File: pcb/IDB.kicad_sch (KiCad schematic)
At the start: 38 parts, among them J1 Conn_01x10_Socket, J10 Conn_01x03_Socket, J11 Conn_01x03_Socket, J12 Conn_01x03_Socket, J13 Conn_01x03_Socket, J14 Conn_01x03_Socket, J15 Conn_01x03_Socket, J16 Conn_01x03_Socket, J17 Conn_01x03_Socket, J18 Conn_01x03_Socket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

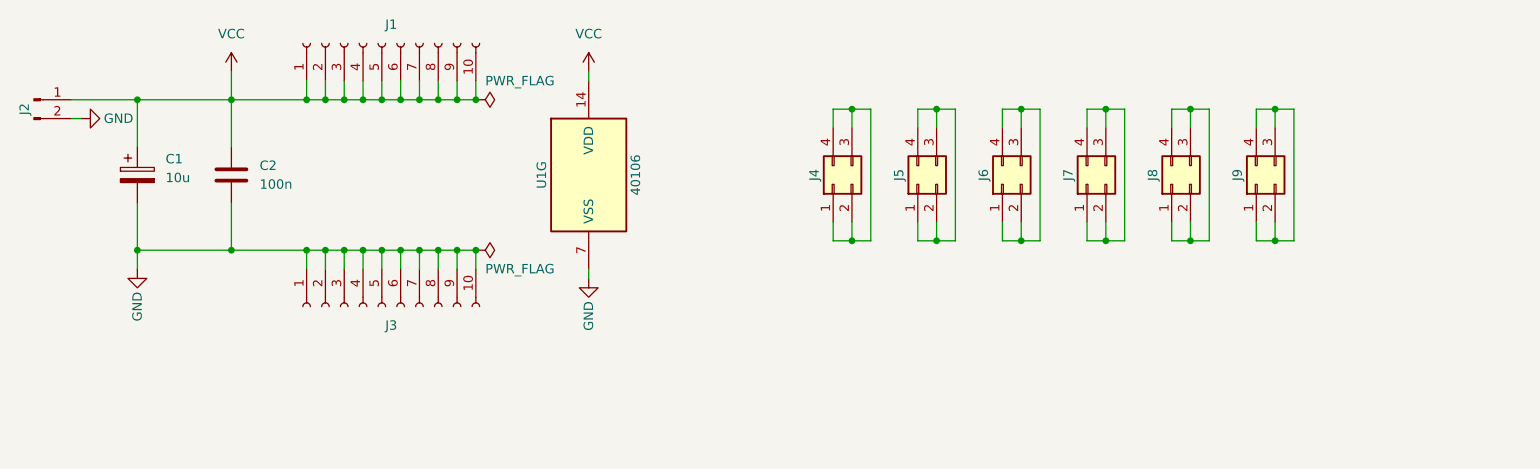
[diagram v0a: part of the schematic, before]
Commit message: Add reverse polarity protection
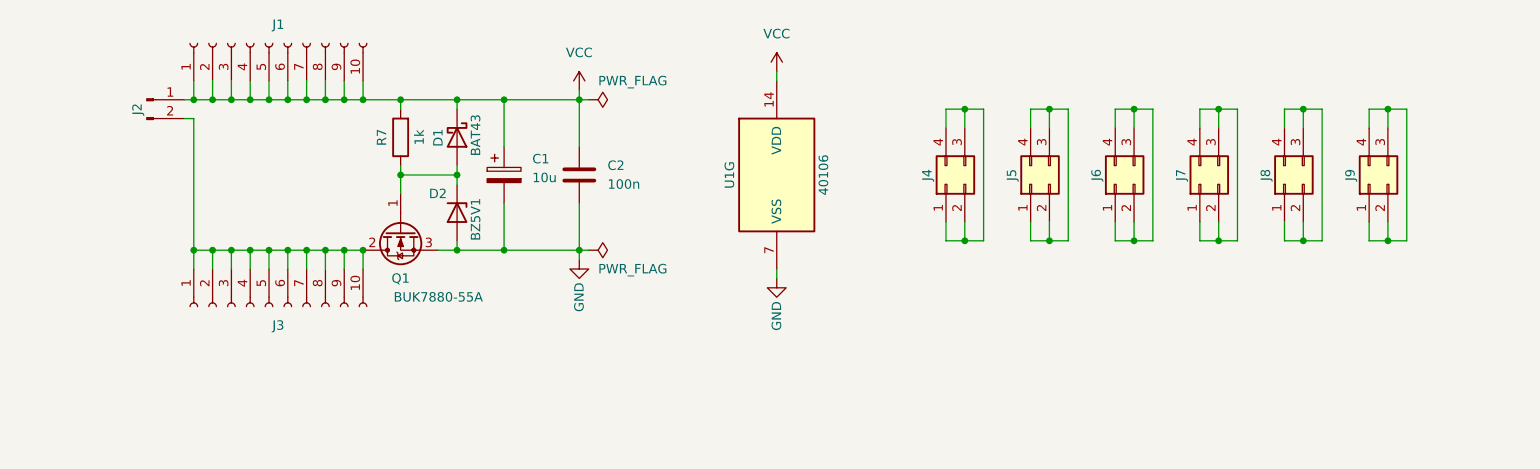
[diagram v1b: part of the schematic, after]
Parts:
- added D1: BAT43, Diode_SMD:D_MiniMELF, symbol Device:D_Schottky
- added D2: BZ5V1, Diode_SMD:D_MiniMELF, symbol Diode:BZV55B15
- added Q1: BUK7880-55A, Package_TO_SOT_SMD:SOT-223-3_TabPin2, symbol Transistor_FET:BUK7880-55A
- added R7: 1k, Resistor_SMD:R_1206_3216Metric, symbol Device:R
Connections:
- net GND: now also D2.2 (A), Q1.3 (S); no longer J2.2 (Pin_2), J3.1 (Pin_1), J3.10 (Pin_10), J3.2 (Pin_2), J3.3 (Pin_3), J3.4 (Pin_4), J3.5 (Pin_5), J3.6 (Pin_6), J3.7 (Pin_7), J3.8 (Pin_8), J3.9 (Pin_9)
- net VCC: now also D1.1 (K), R7.2
- new net: D1.2 (A), D2.1 (K), Q1.1 (G), R7.1
- new net: J2.2 (Pin_2), J3.1 (Pin_1), J3.10 (Pin_10), J3.2 (Pin_2), J3.3 (Pin_3), J3.4 (Pin_4), J3.5 (Pin_5), J3.6 (Pin_6), J3.7 (Pin_7), J3.8 (Pin_8), J3.9 (Pin_9), Q1.2 (D)
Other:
- moved on the sheet: C1, C2, J1, J2, J3, J4, J5, J6, J7, J8, J9, U1G

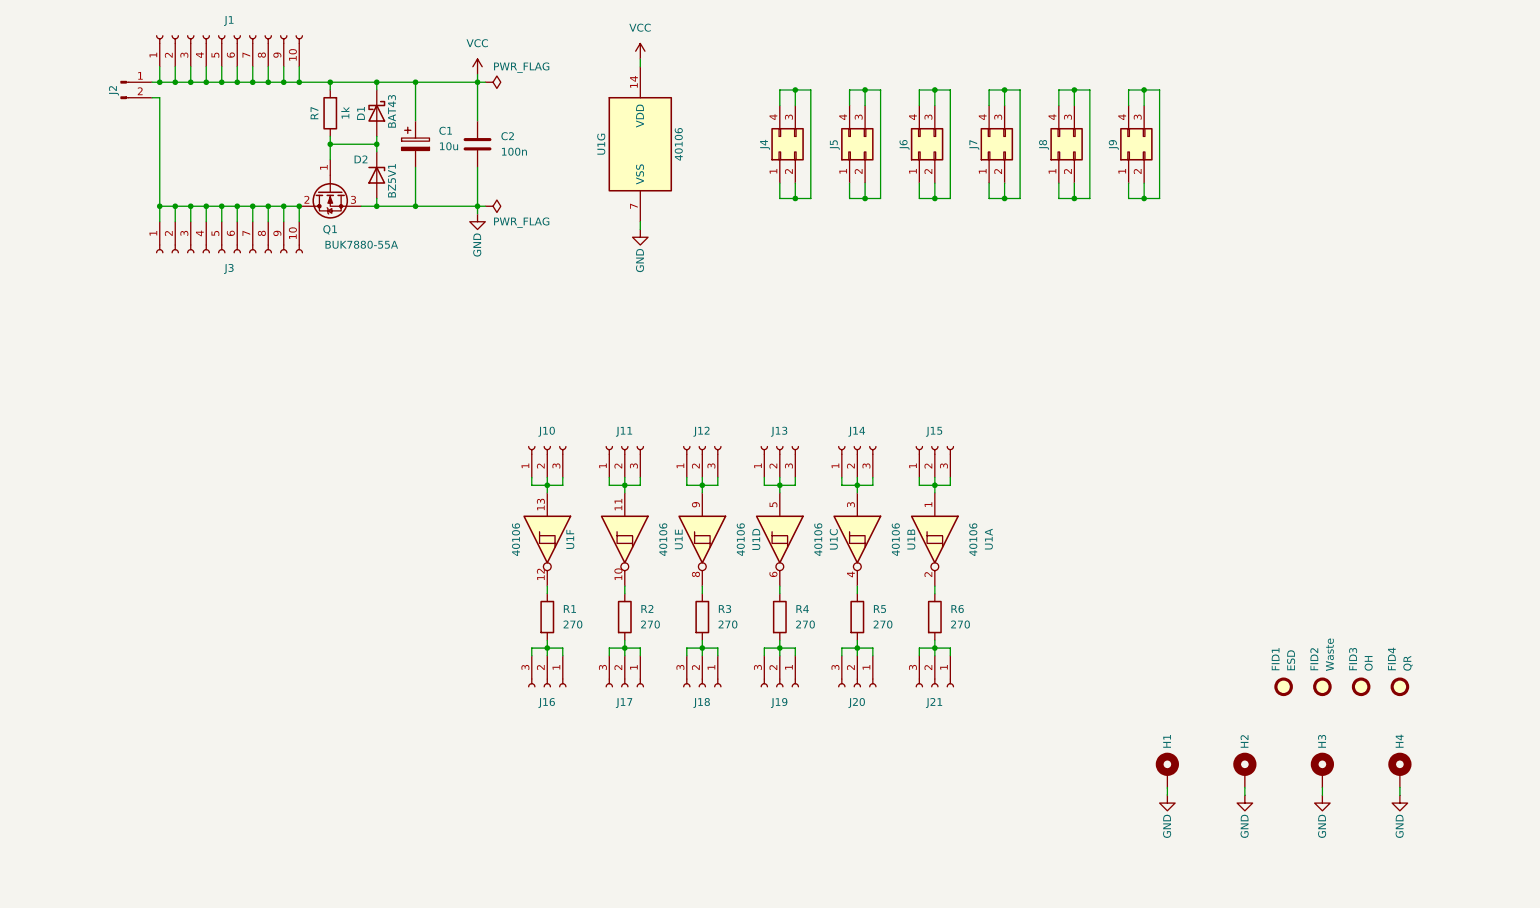
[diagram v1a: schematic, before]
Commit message: Add push/pull possibility for inputs
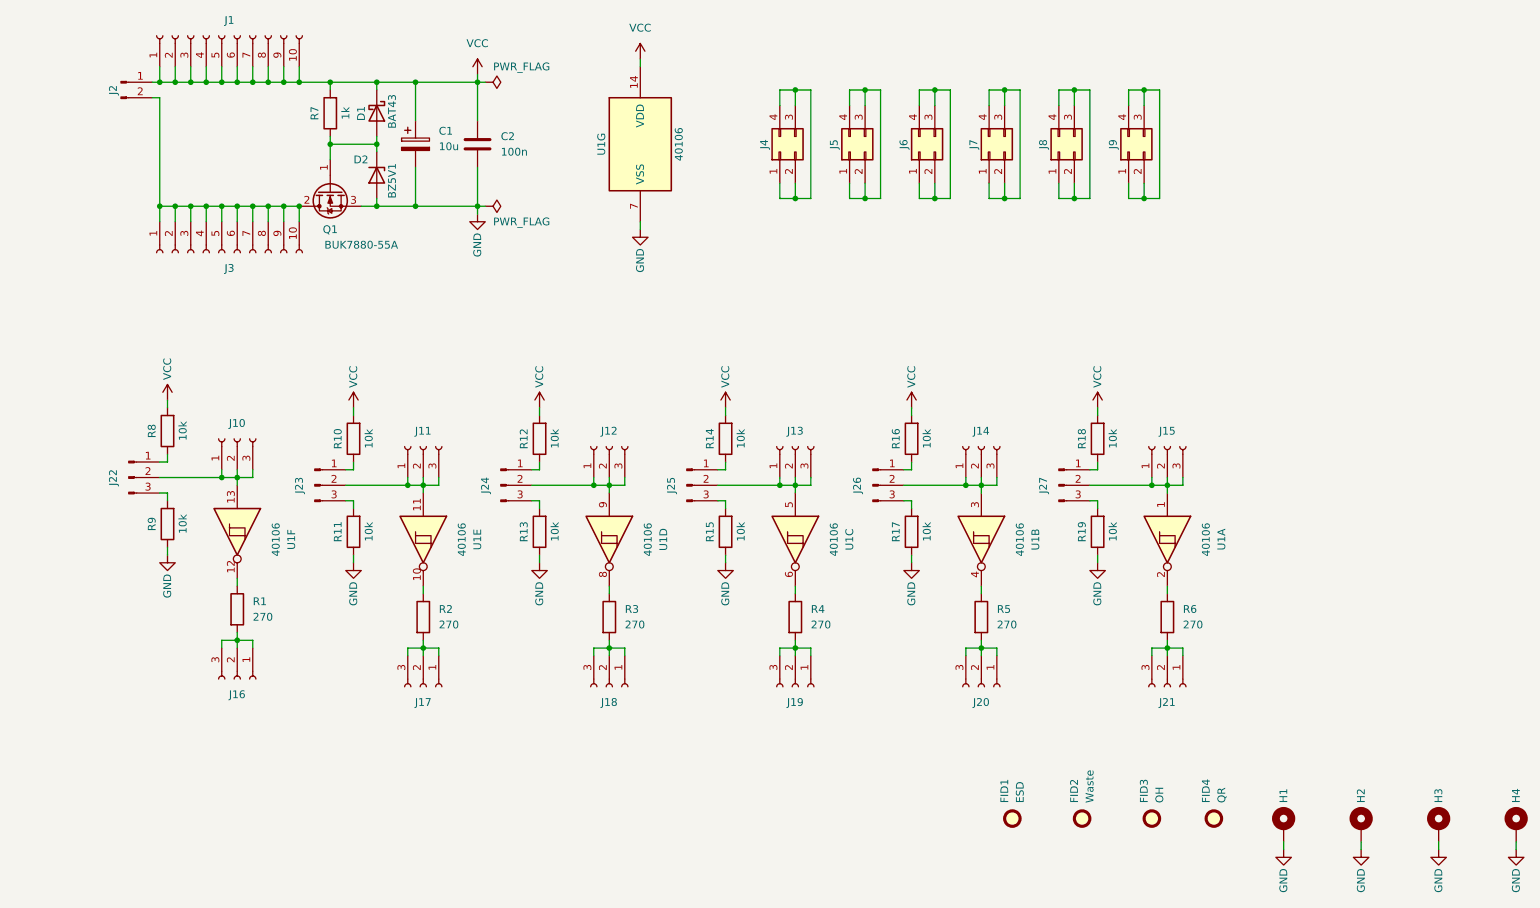
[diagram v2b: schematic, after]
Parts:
- added J22, J23, J24, J25, J26, J27: Conn_01x03_Pin, Connector_PinHeader_2.54mm:PinHeader_1x03_P2.54mm_Vertical, symbol Connector:Conn_01x03_Pin
- added R10, R11, R12, R13, R14, R15, R16, R17, R18, R19, R8, R9: 10k, Resistor_SMD:R_1206_3216Metric, symbol Device:R
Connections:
- net GND: now also R11.1, R13.1, R15.1, R17.1, R19.1, R9.1
- net VCC: now also R10.2, R12.2, R14.2, R16.2, R18.2, R8.2
- net at J12.1 (Pin_1), J12.2 (Pin_2), J12.3 (Pin_3)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: now also J24.2 (Pin_2)
- net at J15.1 (Pin_1), J15.2 (Pin_2), J15.3 (Pin_3)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: now also J27.2 (Pin_2)
- net at J11.1 (Pin_1), J11.2 (Pin_2), J11.3 (Pin_3)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: now also J23.2 (Pin_2)
- net at J13.1 (Pin_1), J13.2 (Pin_2), J13.3 (Pin_3)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: now also J25.2 (Pin_2)
- net at J14.1 (Pin_1), J14.2 (Pin_2), J14.3 (Pin_3)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: now also J26.2 (Pin_2)
- net at J10.1 (Pin_1), J10.2 (Pin_2), J10.3 (Pin_3)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: now also J22.2 (Pin_2)
- new net: J25.1 (Pin_1), R14.1
- new net: J26.1 (Pin_1), R16.1
- new net: J26.3 (Pin_3), R17.2
- new net: J24.1 (Pin_1), R12.1
- new net: J27.1 (Pin_1), R18.1
- new net: J24.3 (Pin_3), R13.2
- new net: J25.3 (Pin_3), R15.2
- new net: J27.3 (Pin_3), R19.2
- new net: J23.1 (Pin_1), R10.1
- new net: J23.3 (Pin_3), R11.2
- new net: J22.1 (Pin_1), R8.1
- new net: J22.3 (Pin_3), R9.2
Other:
- moved on the sheet: FID1, FID2, FID3, FID4, H1, H2, H3, H4, J10, J11, J12, J13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

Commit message: Rename/Add/Remove bom fields
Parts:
- C1: HTL (none) -> 100354; Vendor HTL -> (none); VendorId 100354 -> (none)
- C2: HTL (none) -> 100128; Vendor HTL -> (none); VendorId 100128 -> (none)
- D1: HTL (none) -> 100206; Vendor HTL -> (none); VendorId 100206 -> (none)
- D2: HTL (none) -> 100193; Vendor HTL -> (none); VendorId 100193 -> (none)
- FID1, FID2, FID3, FID4: now left out of the parts list
- H1, H2, H3, H4: HTL (none) -> 101018, 101382; Vendor HTL -> (none); VendorId 101018, 101382 -> (none)
- J1, J3: DigiKey (none) -> 2057-RS1-10-G-ND; Vendor DigiKey -> (none); VendorId 2057-RS1-10-G-ND -> (none)
- J10, J11, J12, J13, J14, J15, J16, J17, J18, J19, J20, J21: DigiKey (none) -> 2057-RS1-03-G-ND; Vendor DigiKey -> (none); VendorId 2057-RS1-03-G-ND -> (none)
- J2: HTL (none) -> 101521; Vendor HTL -> (none); VendorId 101521 -> (none)
- J22, J23, J24, J25, J26, J27: HTL (none) -> 101521, 6 x 102854; Vendor HTL -> (none); VendorId 101521, 6 x 102854 -> (none)
- J4, J5, J6, J7, J8, J9: DigiKey (none) -> 2057-RS2-04-G-ND; Vendor DigiKey -> (none); VendorId 2057-RS2-04-G-ND -> (none)
- Q1: HTL (none) -> 103520; Vendor HTL -> (none); VendorId 103520 -> (none)
- R1, R2, R3, R4, R5, R6: HTL (none) -> 102938; Vendor HTL -> (none); VendorId 102938 -> (none)
- R10, R11, R12, R13, R14, R15, R16, R17, R18, R19, R8, R9: HTL (none) -> 102967; Vendor HTL -> (none); VendorId 102967 -> (none)
- R7: HTL (none) -> 102951; Vendor HTL -> (none); VendorId 102951 -> (none)
- U1: DigiKey (none) -> 296-14081-1-ND; Vendor DigiKey -> (none); VendorId 296-14081-1-ND -> (none)
